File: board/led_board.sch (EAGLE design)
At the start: 18 parts

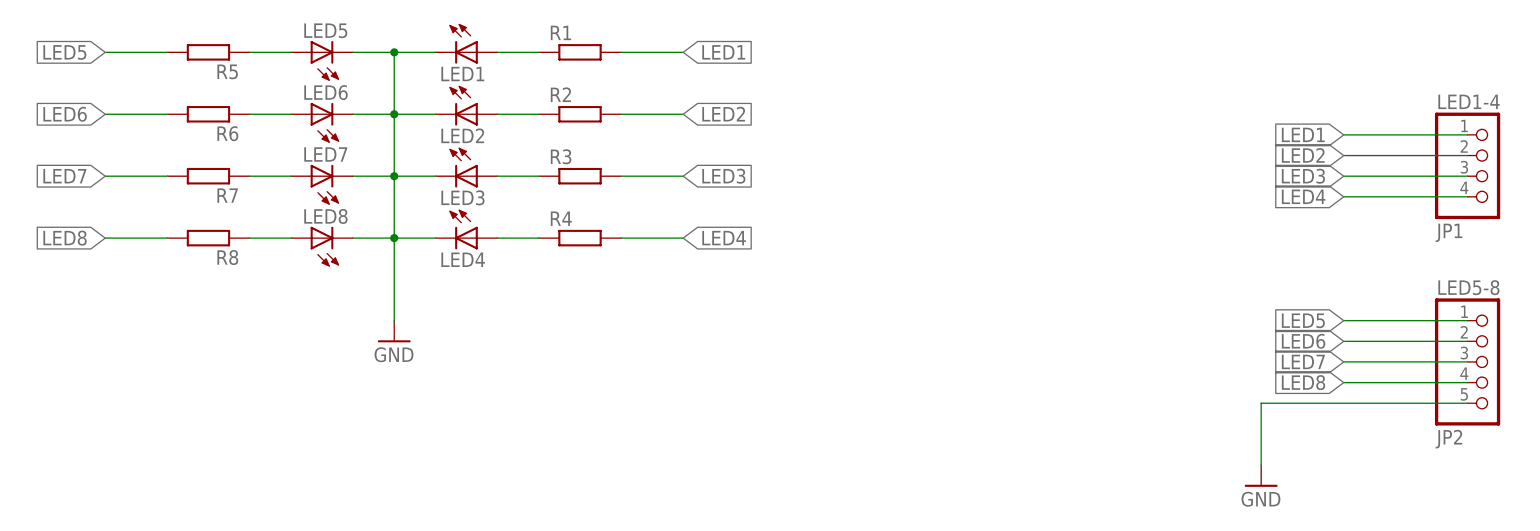
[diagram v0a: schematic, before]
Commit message: added values to resistors on led board
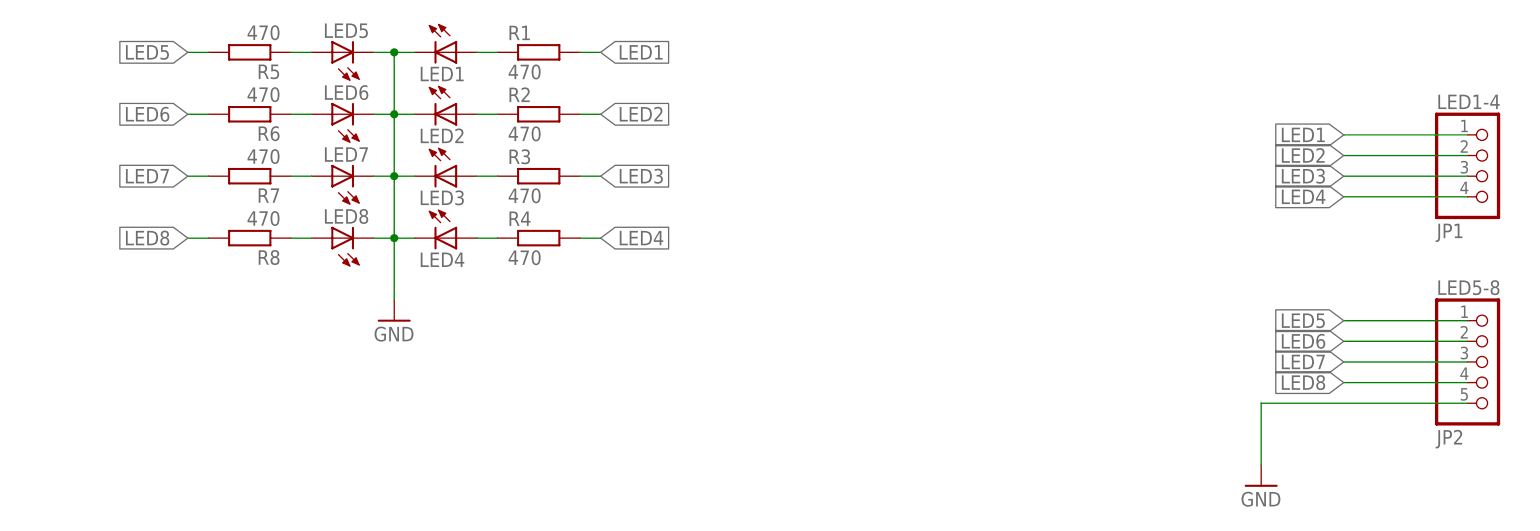
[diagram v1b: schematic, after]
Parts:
- R1, R2, R3, R4, R5, R6, R7, R8: value (none) -> 470
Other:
- moved on the sheet: LED1, LED2, LED3, LED4, LED5, LED6, LED7, LED8, R1, R2, R3, R4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
